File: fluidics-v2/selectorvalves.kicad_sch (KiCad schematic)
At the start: 35 parts, among them IC1 MCZ33996EKR2

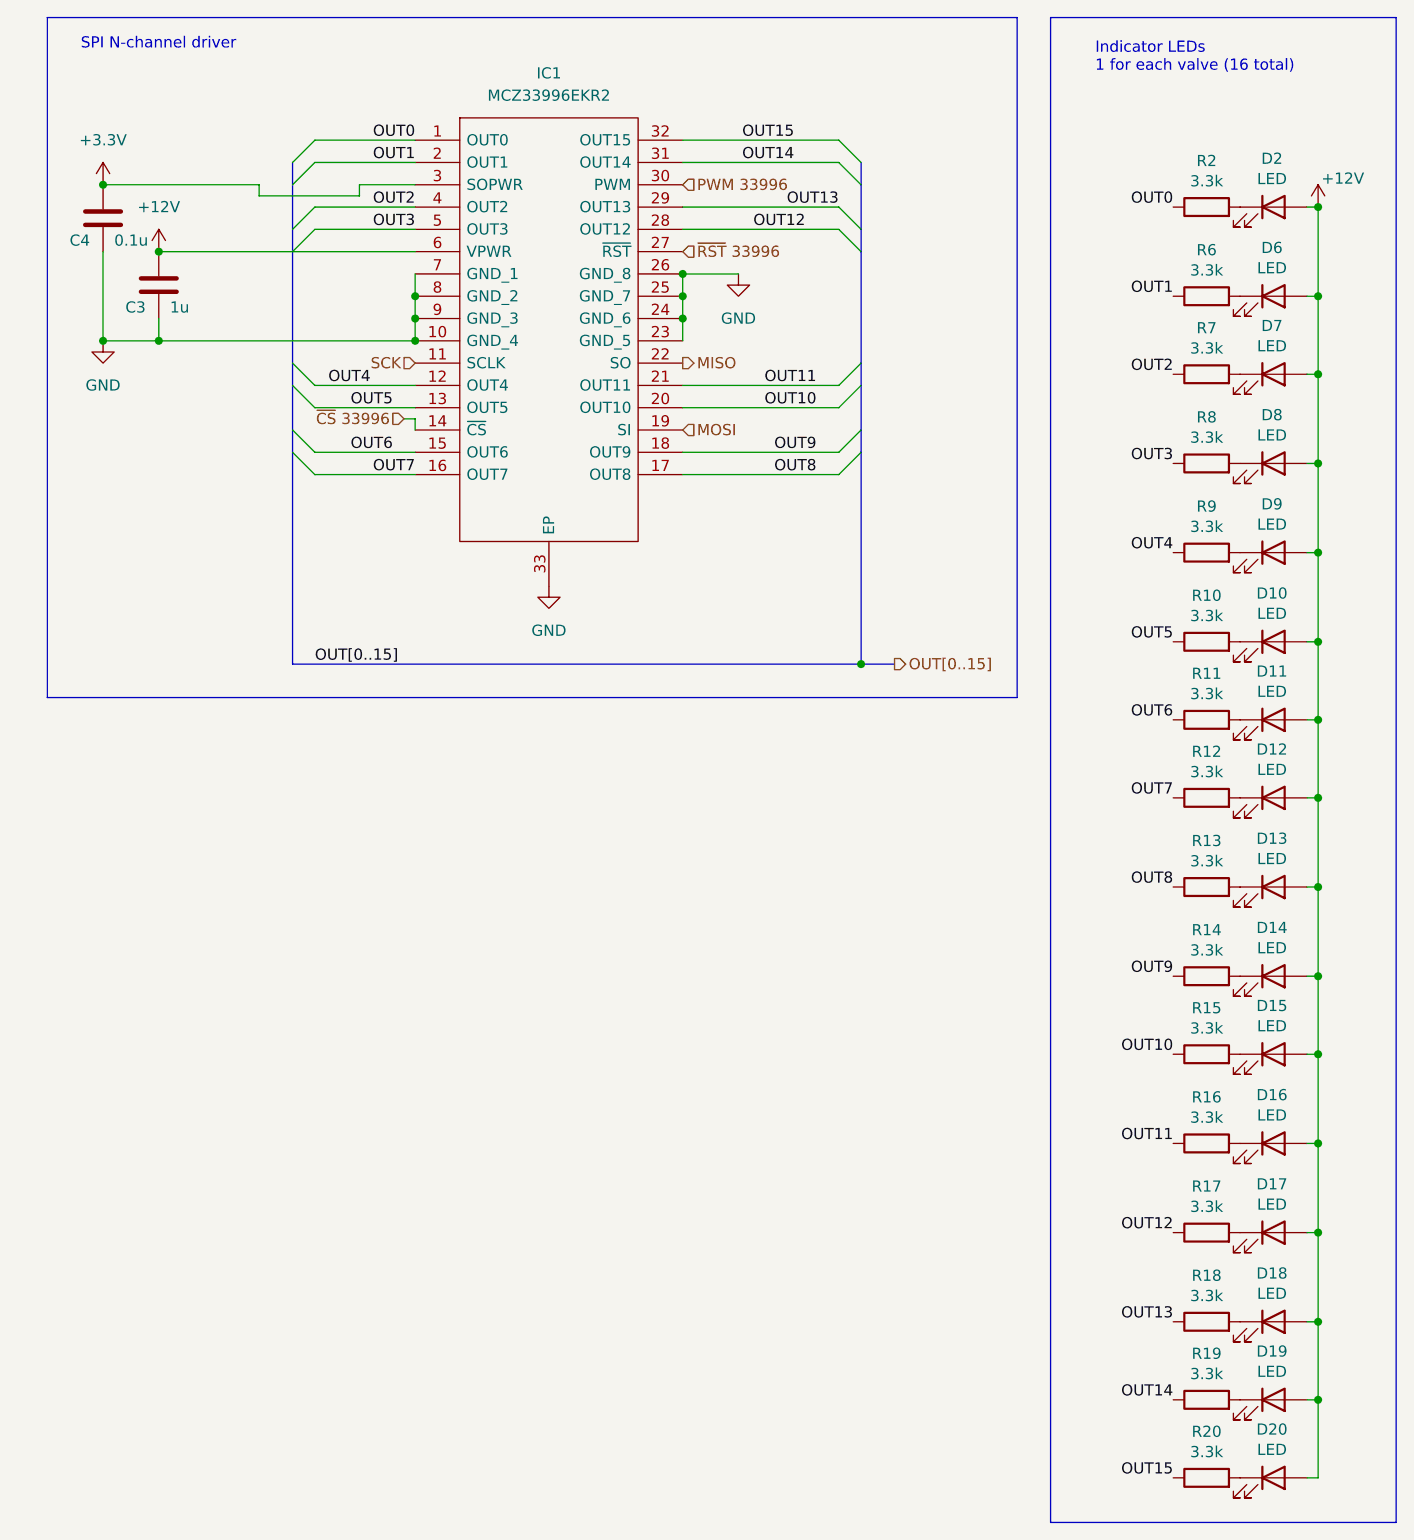
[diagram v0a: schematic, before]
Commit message: added footprints and mounting holes, cleaned up some sheets
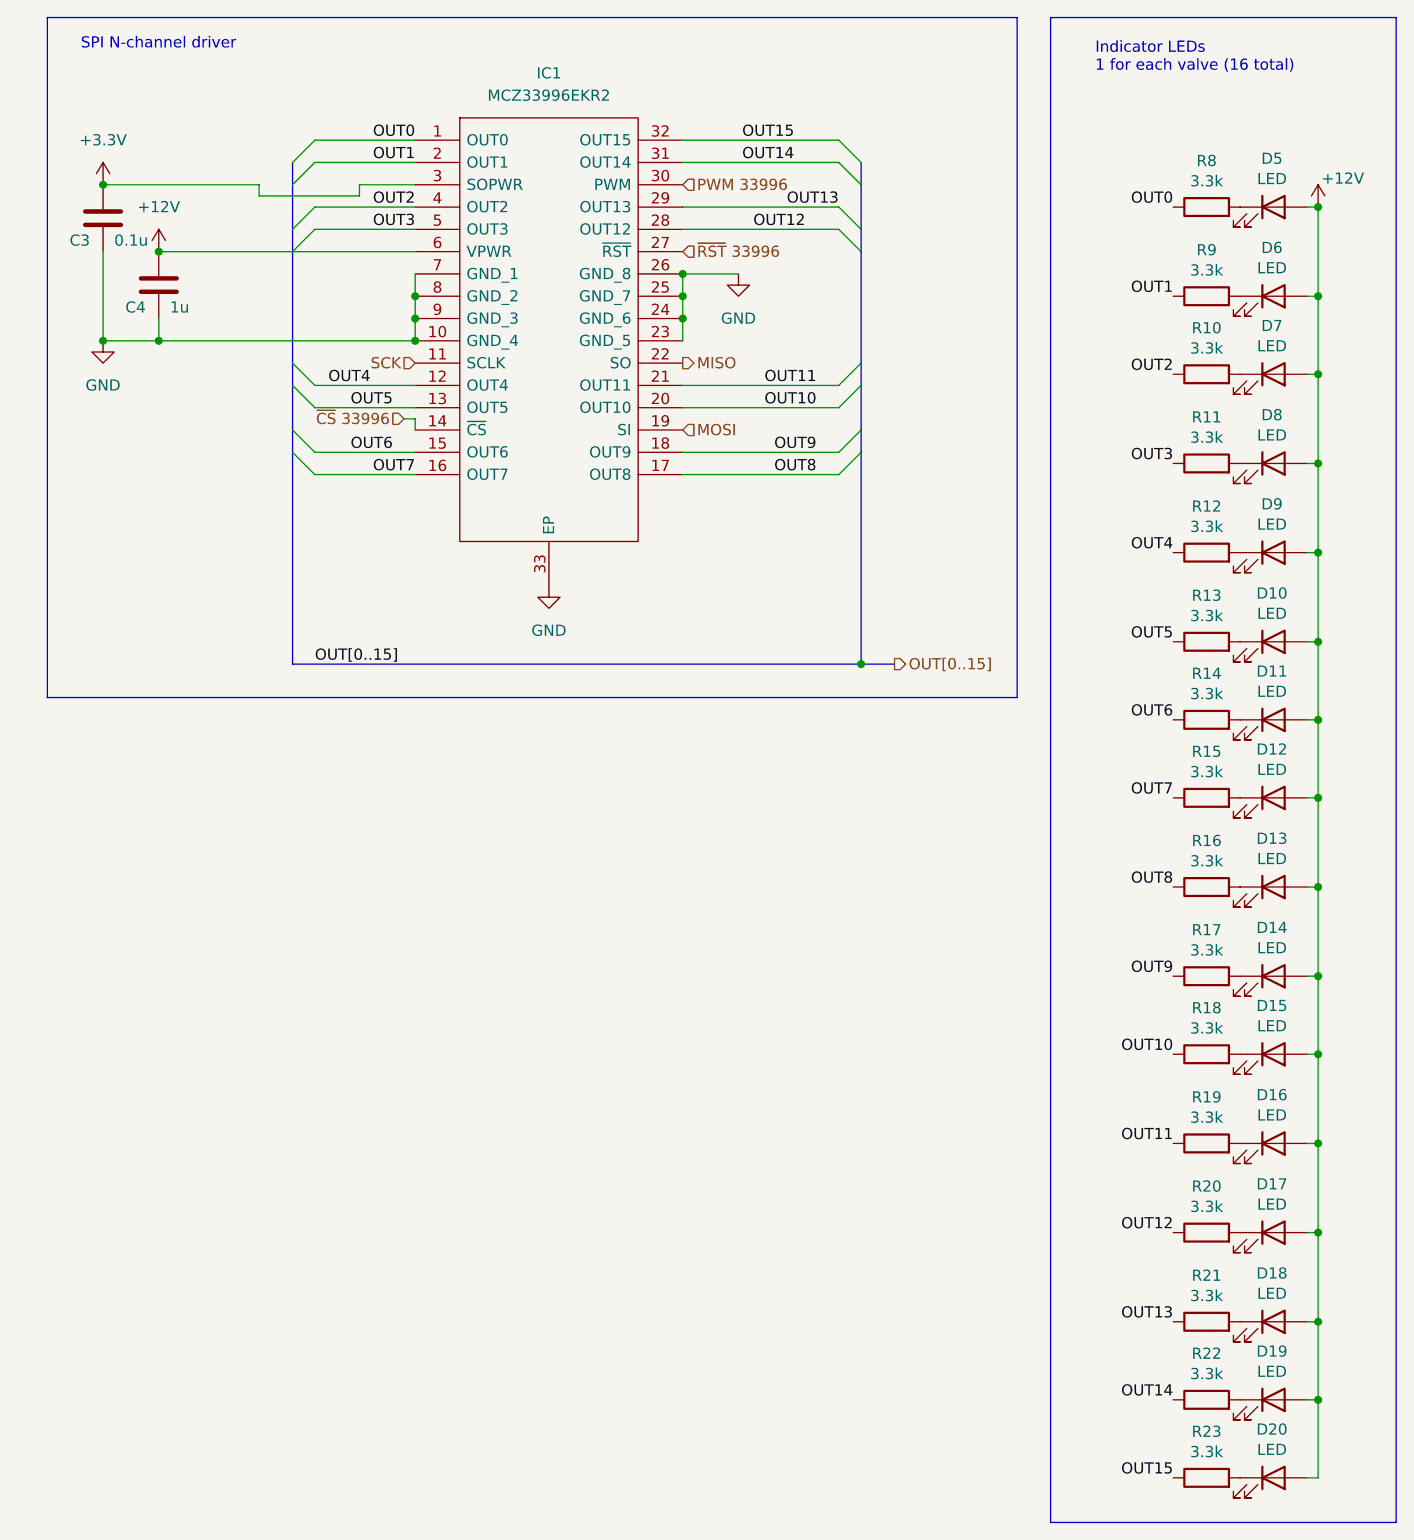
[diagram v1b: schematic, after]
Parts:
- renumbered C4 to C3, C3 to C4, D2 to D5, R7 to R10, R8 to R11, R9 to R12, R10 to R13, R11 to R14, R12 to R15, R13 to R16, R14 to R17, R15 to R18, R16 to R19, R17 to R20, R18 to R21, R19 to R22, R20 to R23, R2 to R8, R6 to R9

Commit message: started layout
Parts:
- renumbered C3 to C4, C4 to C5

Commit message: added pressure controllers and more flow sensors
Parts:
- C5: footprint Capacitor_SMD:C_0603_1608Metric -> Capacitor_SMD:C_0805_2012Metric
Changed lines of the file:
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@@
       (effects (font (size 1.27 1.27)) (justify left))
     )
-    (property "Footprint" "Capacitor_SMD:C_0603_1608Metric" (at 28.9052 49.53 0)
+    (property "Footprint" "Capacitor_SMD:C_0805_2012Metric" (at 28.9052 49.53 0)
       (effects (font (size 1.27 1.27)) hide)
     )

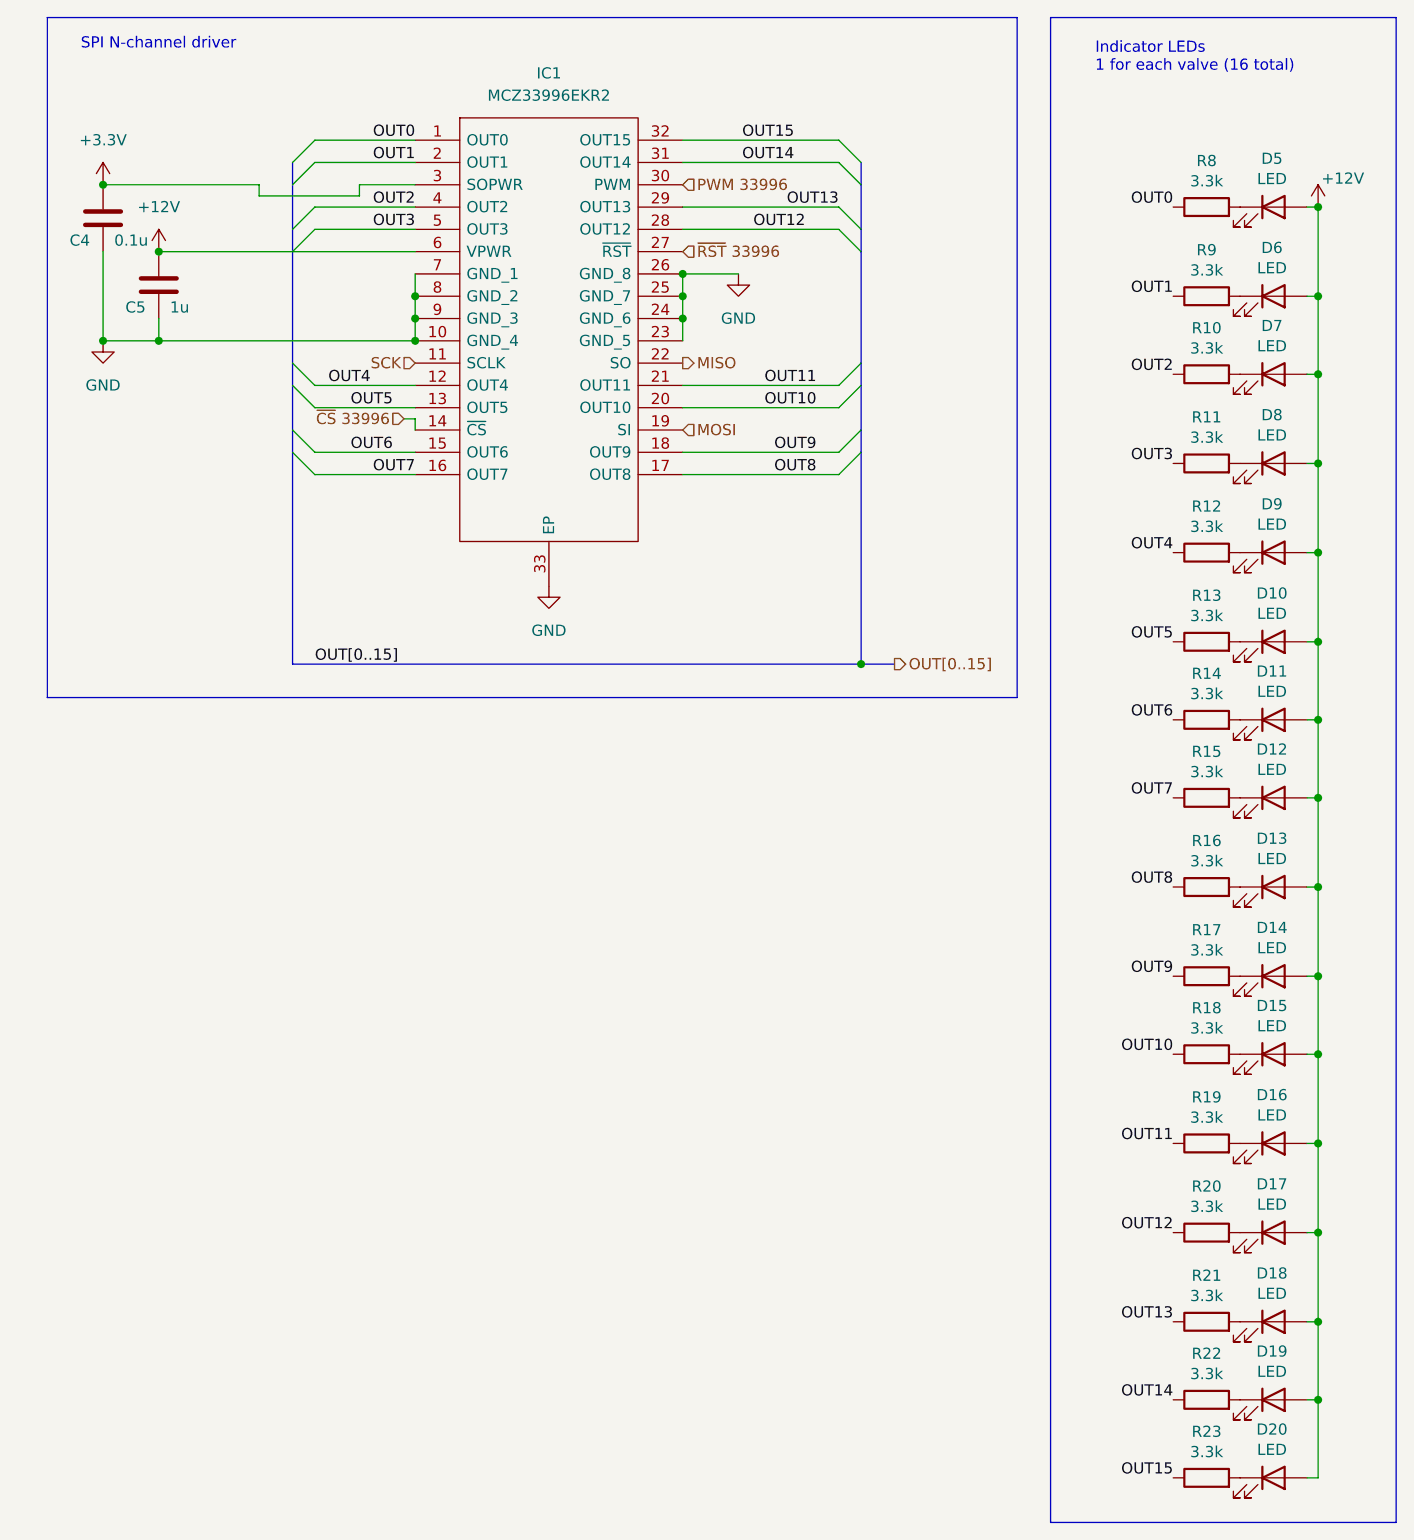
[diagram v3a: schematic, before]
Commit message: added new connector for motor control daughter board. began layout
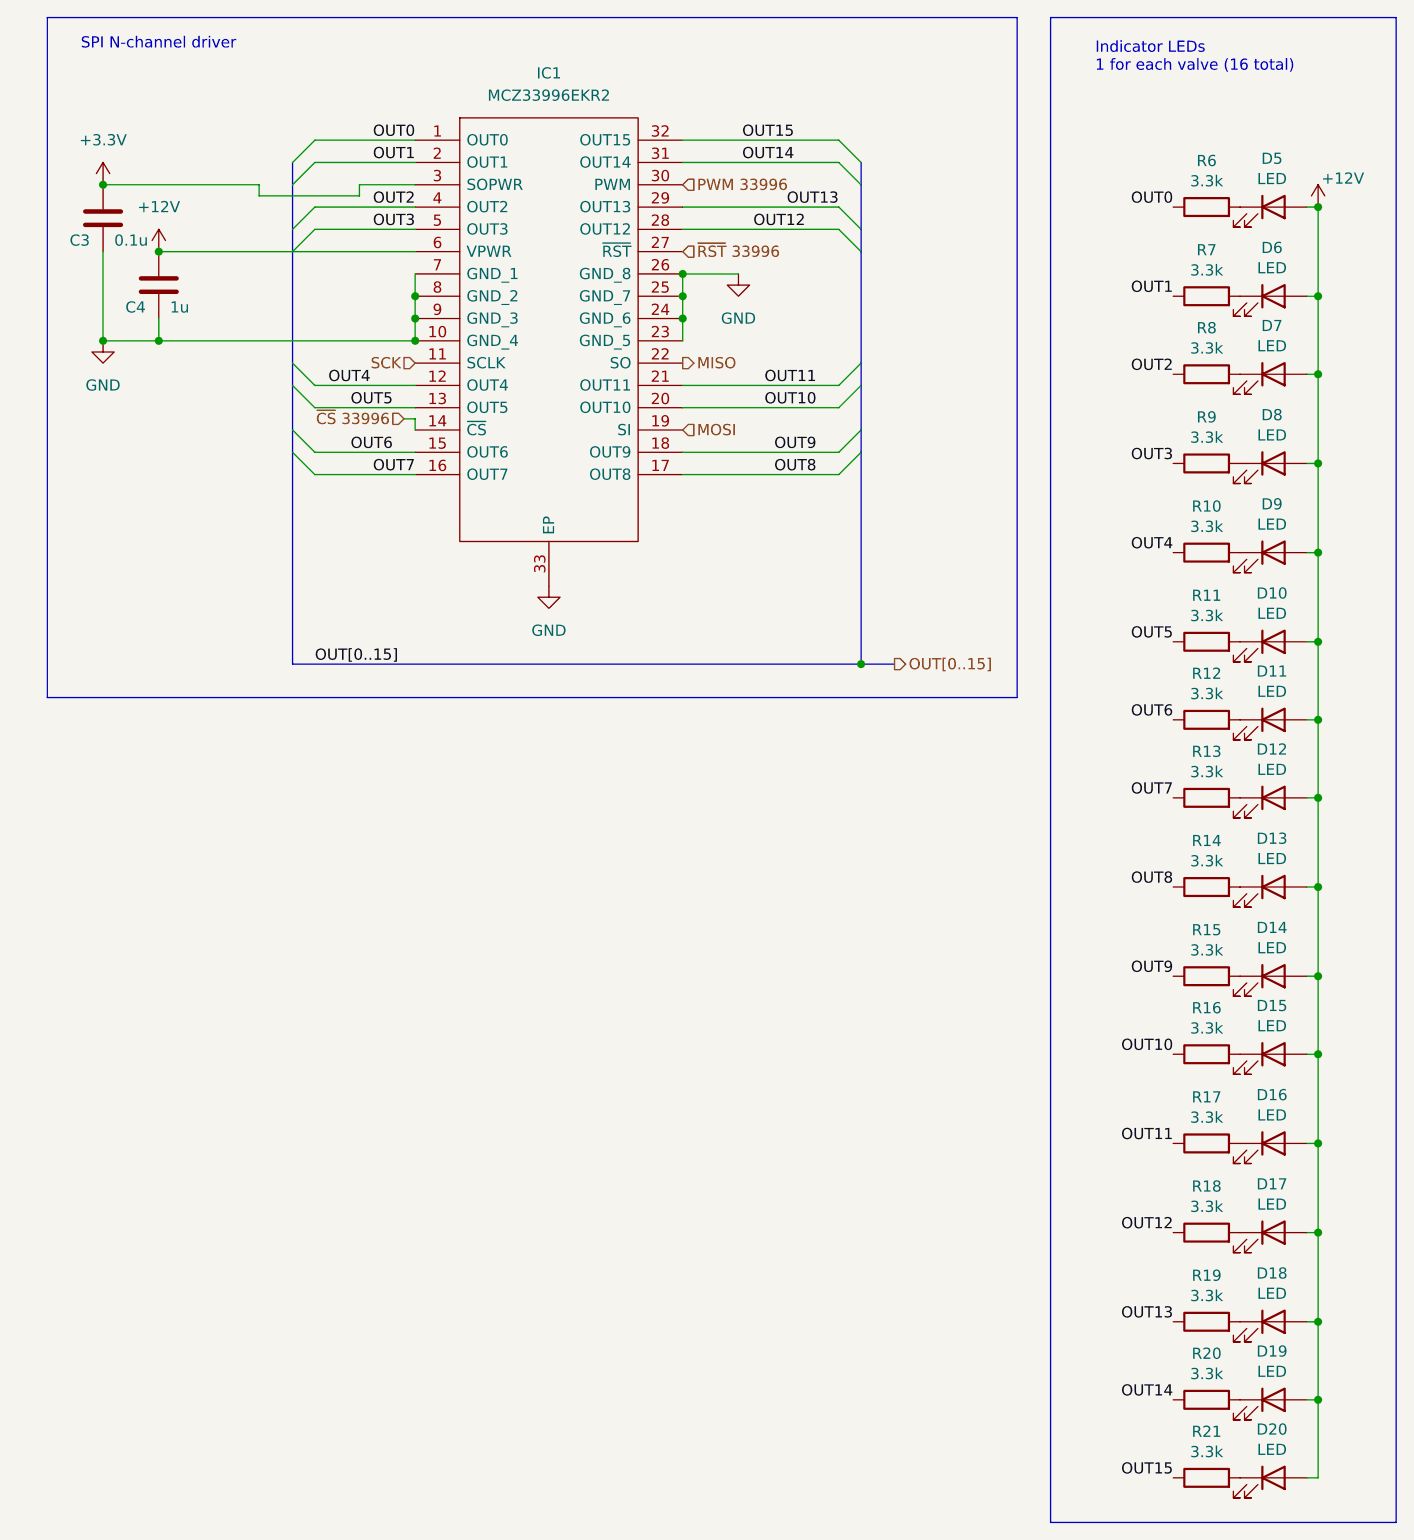
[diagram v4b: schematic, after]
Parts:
- renumbered C4 to C3, C5 to C4, R12 to R10, R13 to R11, R14 to R12, R15 to R13, R16 to R14, R17 to R15, R18 to R16, R19 to R17, R20 to R18, R21 to R19, R22 to R20, R23 to R21, R8 to R6, R9 to R7, R10 to R8, R11 to R9
